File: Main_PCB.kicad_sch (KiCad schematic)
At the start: 63 parts, among them IC1 TCN75AVUA713-VAO, J1 Conn_Coaxial, J2 Conn_02x03_Odd_Even, J3 USB_C_Receptacle_USB2.0, J4 Conn_01x03_Male, J5 Conn_01x08, J6 Conn_01x08, SW1 SW_Push, U1 LTR-329ALS-01, U2 RFM95W-868S2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

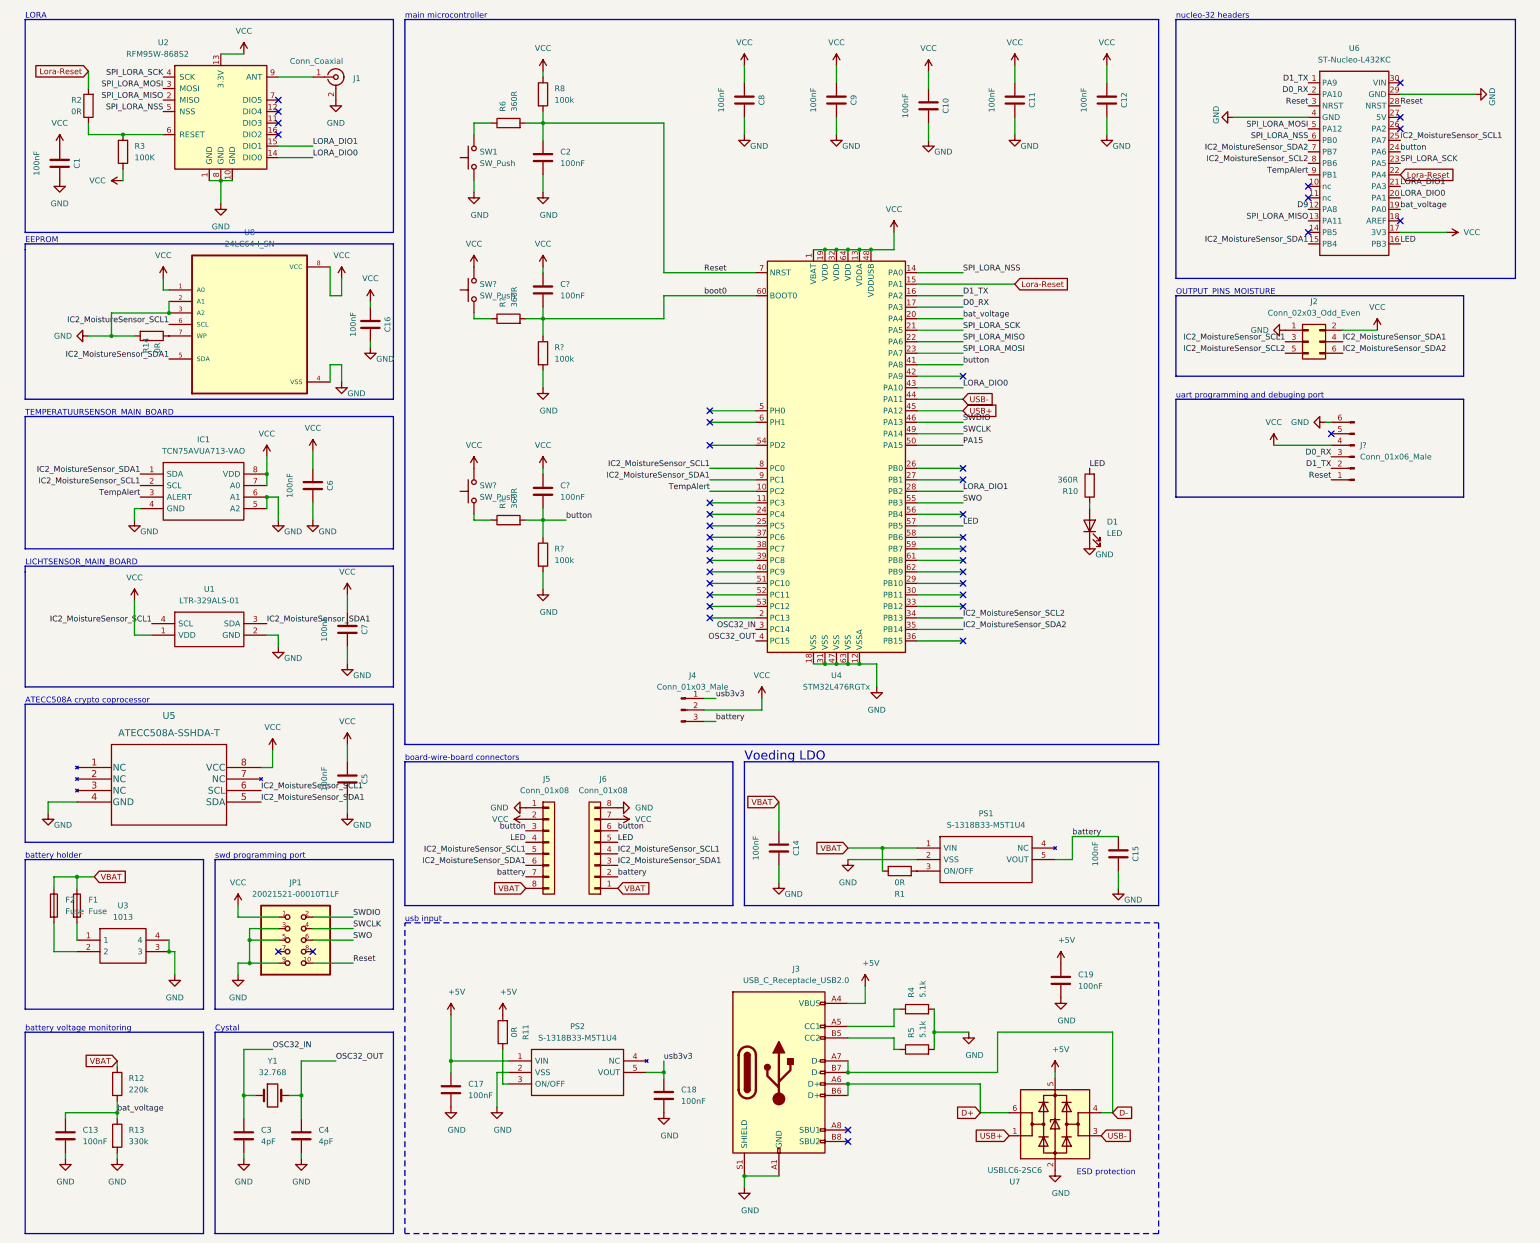
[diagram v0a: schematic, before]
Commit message: updated ldo
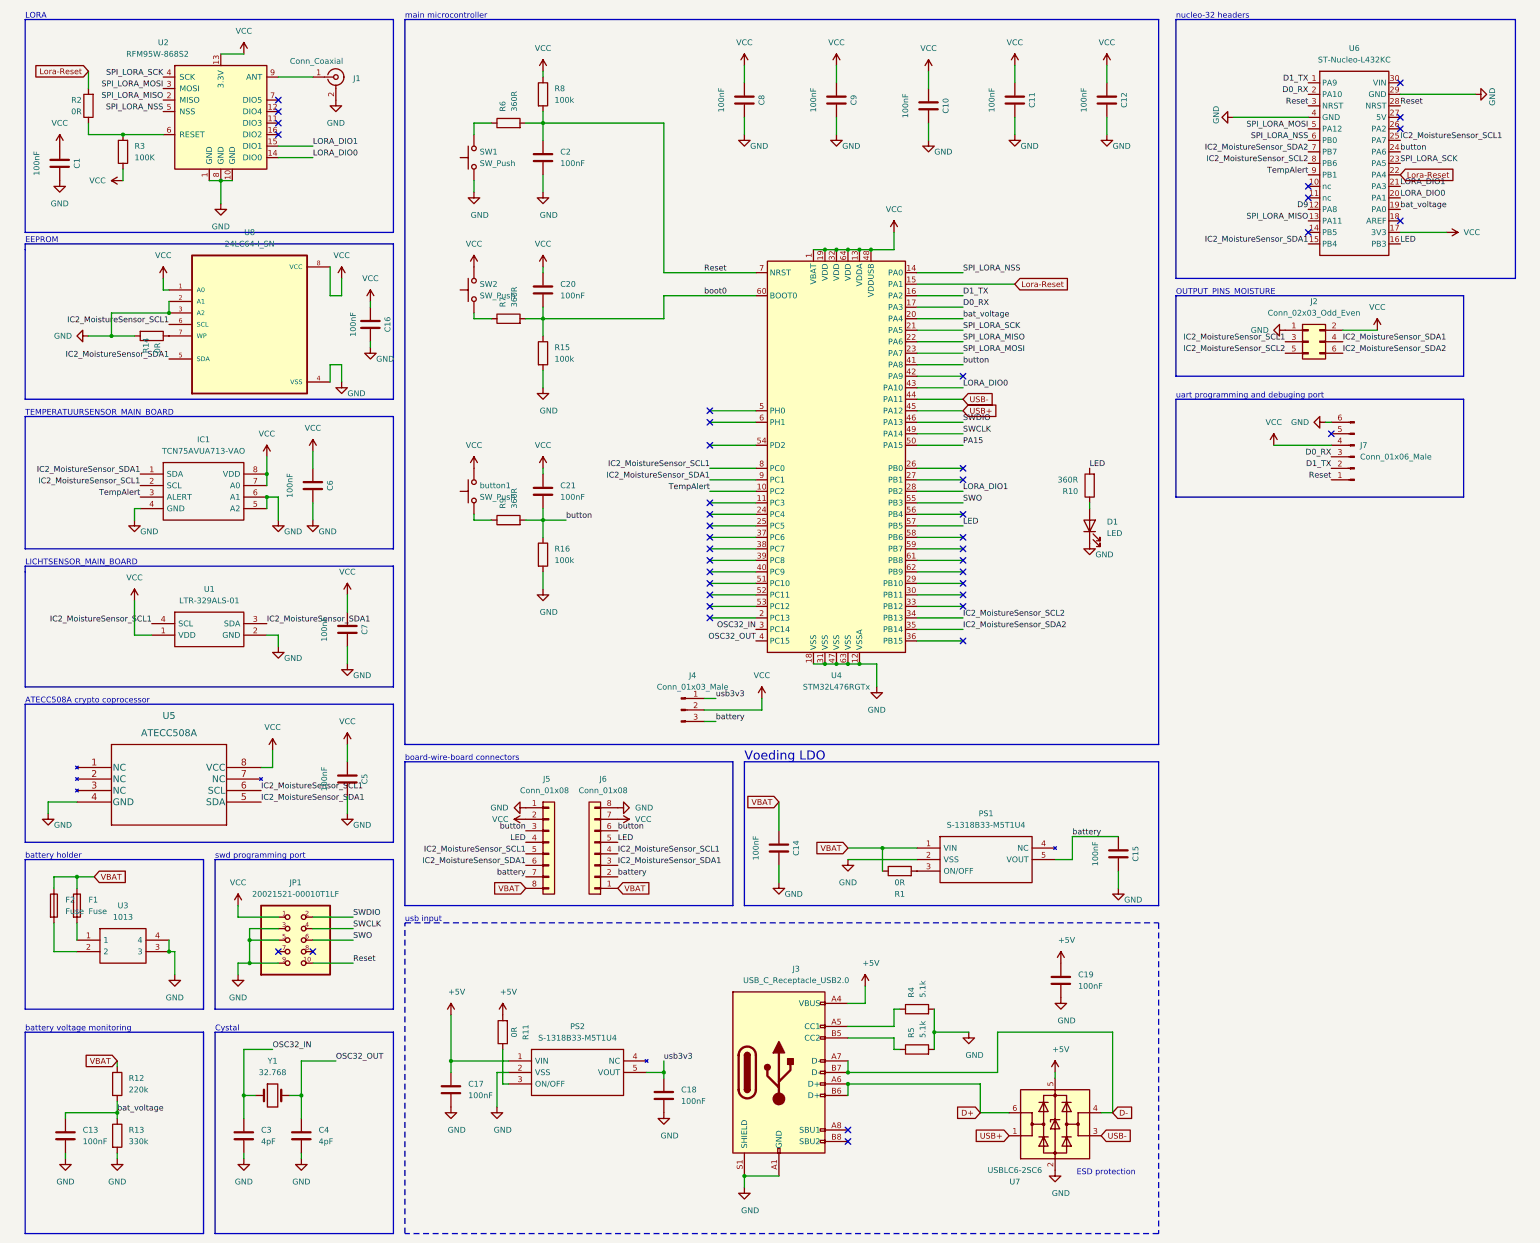
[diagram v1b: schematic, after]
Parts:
- C13, C17, C18, C19, C2: footprint Capacitor_SMD:C_0805_2012Metric_Pad1.18x1.45mm_HandSolder -> Capacitor_SMD:C_0603_1608Metric_Pad1.08x0.95mm_HandSolder
- C20, C21: renamed from C?; footprint Capacitor_SMD:C_0805_2012Metric_Pad1.18x1.45mm_HandSolder -> Capacitor_SMD:C_0603_1608Metric_Pad1.08x0.95mm_HandSolder
- U5: value ATECC508A-SSHDA-T -> ATECC508A
- gave numbers to parts that had none: 7

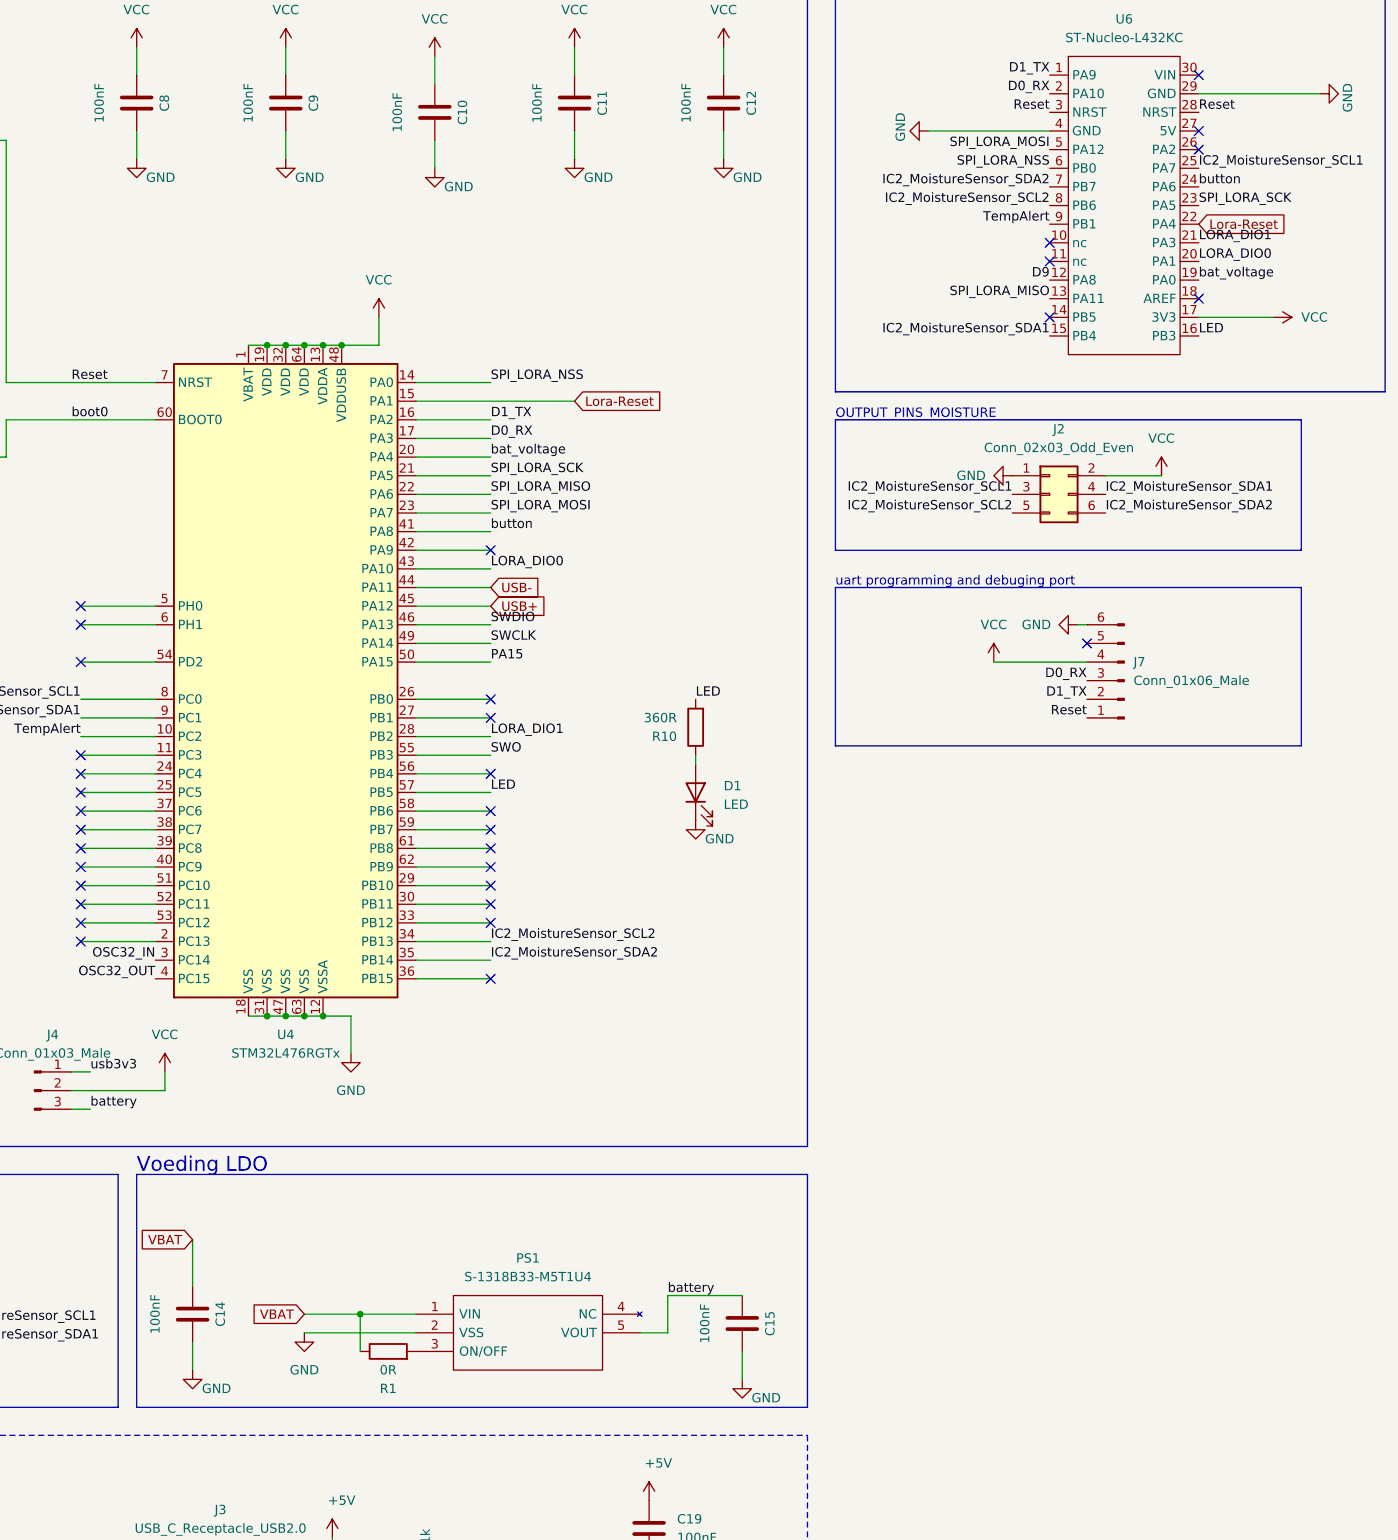
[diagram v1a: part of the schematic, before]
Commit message: updated ldo and fixed git mistake
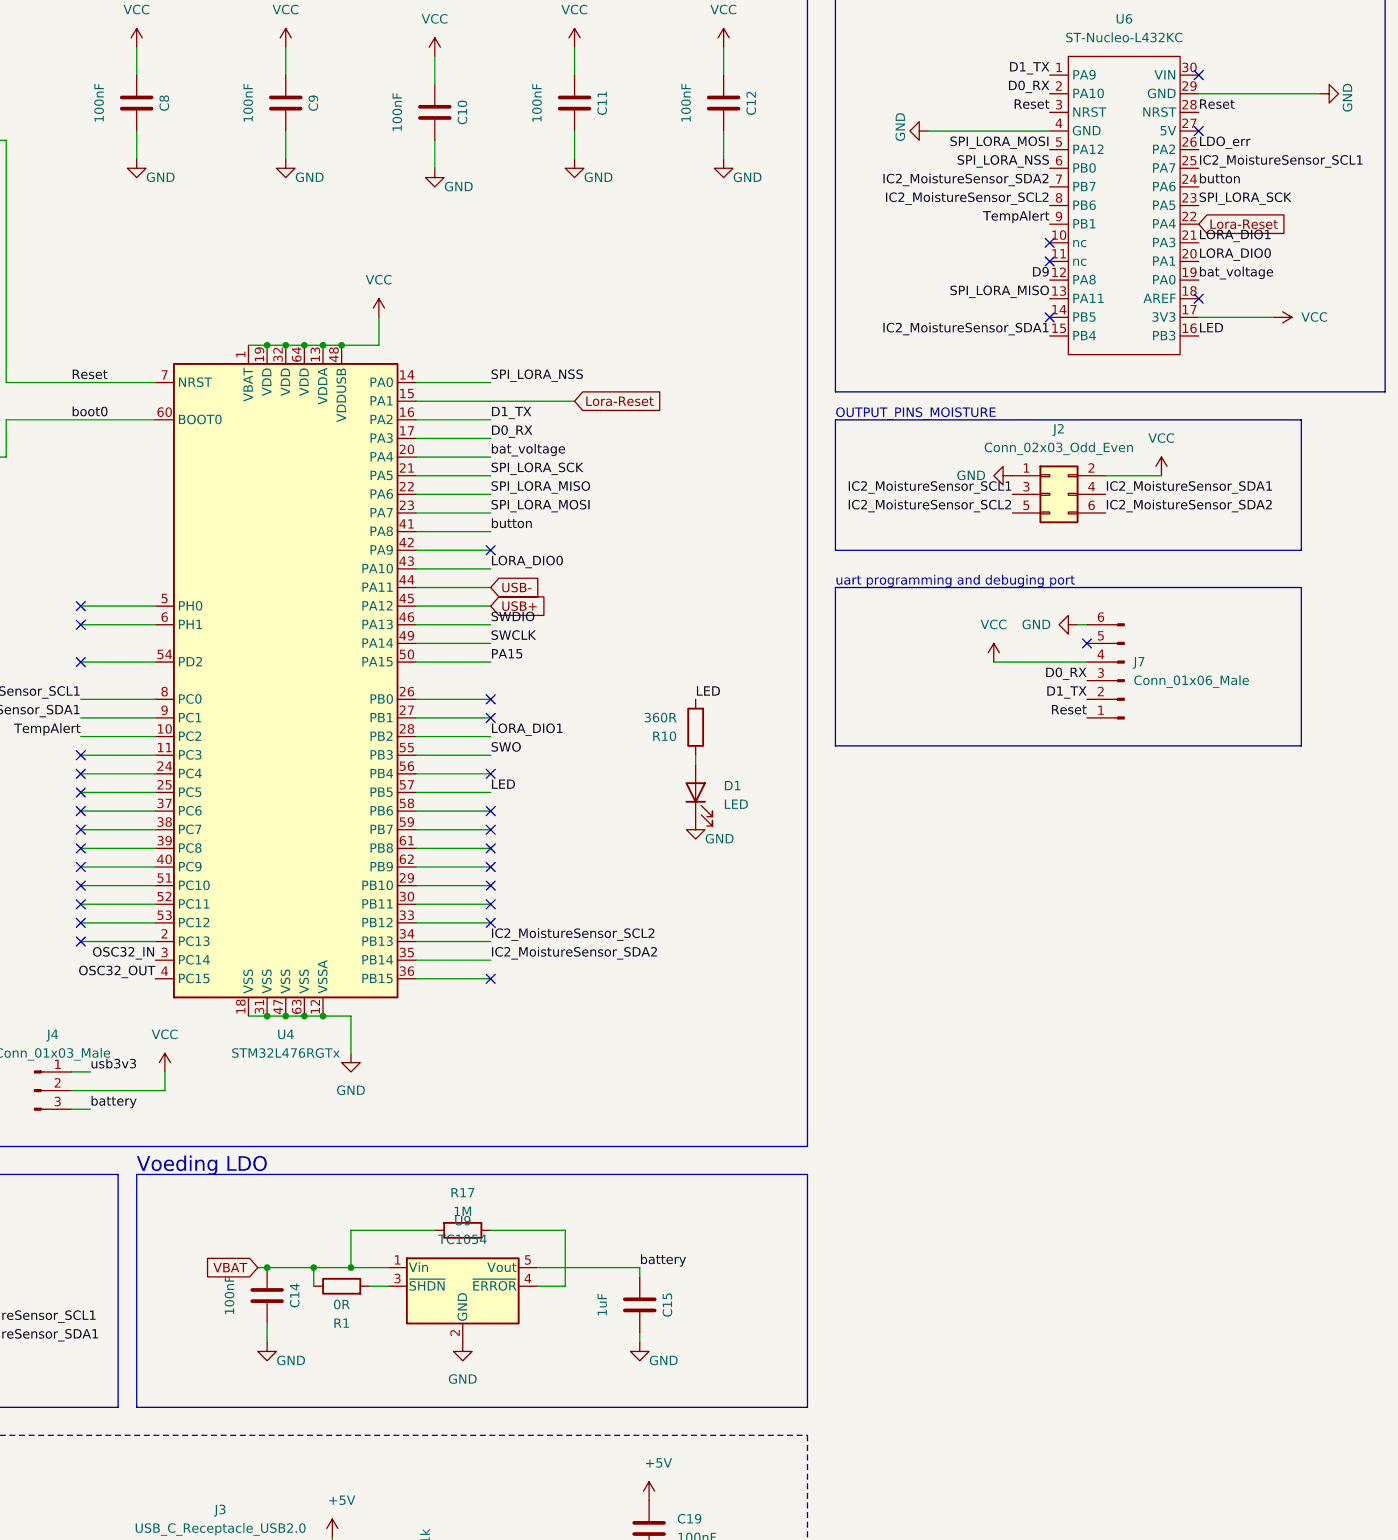
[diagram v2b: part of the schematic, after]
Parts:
- removed PS1: S-1318B33-M5T1U4, S-1318B33:SOT95P275X130-5N, symbol S-1318B33-M5T1U4:S-1318B33-M5T1U4
- added R17: 1M, Resistor_SMD:R_0603_1608Metric_Pad0.98x0.95mm_HandSolder, symbol Device:R
- added U9: TC1054, Package_TO_SOT_SMD:SOT-23-5, symbol Regulator_Linear:TC1054
- C15: value 100nF -> 1uF; footprint Capacitor_SMD:C_0603_1608Metric_Pad1.08x0.95mm_HandSolder -> Capacitor_SMD:C_0805_2012Metric_Pad1.18x1.45mm_HandSolder
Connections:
- net GND: now also U9.2 (GND)
- net VBAT: now also R17.2, U9.1 (Vin)
- net battery: now also U9.5 (Vout)
- net LDO_err: now reaches U6.26 (PA2)
- net at R1.2: now also U9.3 (~{SHDN})
- new net: R17.1, U9.4 (~{ERROR})
- no-connect marks 42 -> 41
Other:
- moved on the sheet: C14, C15, R1
